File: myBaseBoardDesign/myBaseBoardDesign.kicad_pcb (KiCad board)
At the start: 2 copper layers, 100 x 100 mm, 14 parts, among them J1 BaseBoard, J2 Barrel_Jack_Switch, J4 Screw_Terminal_01x02, Q2 DMP6180SK3, SW1 SW_SPDT, U1 ESP32-S3-DevKitC

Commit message: Updated Tue Apr 2 2024 18:42
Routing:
- net GND: track 110.4 -> 147.2 mm, vias 83 -> 54
- net GP9: track 104.7 -> 141.4 mm, vias 1 -> 0
- net GP10: track 101.1 -> 136.0 mm, vias 1 -> 0
- net GP13: track 119.5 -> 101.2 mm
- net +5V: track 111.7 -> 128.7 mm, vias 2 -> 0
- net Net-(D1-A): track 21.9 -> 8.09 mm
- net GP46: track 127.9 -> 138.5 mm
- net GP5: track 106.7 -> 96.3 mm
- net GP7: track 87.2 -> 97.0 mm, vias 0 -> 2
- net GP15: track 49.8 -> 41.1 mm, vias 0 -> 1
- net GP16: track 49.8 -> 41.1 mm, vias 0 -> 1
- net GP47: track 76.3 -> 70.0 mm
- net GP40: track 88.6 -> 82.4 mm
- net GP8: track 106.4 -> 100.5 mm
- net GP2: track 91.8 -> 86.6 mm, vias 2 -> 1
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
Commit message: commit Apr 7 2024
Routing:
- net GP46: track 138.5 -> 121.7 mm, vias 0 -> 2
- net GP42: track 76.5 -> 82.6 mm
- net GND: track 147.2 -> 149.6 mm, vias 54 -> 130
- net GP21: track 88.8 -> 89.2 mm, vias 0 -> 1
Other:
- board text added: "+3V3"
- board text added: "+5V"
- board text added: "VIN"

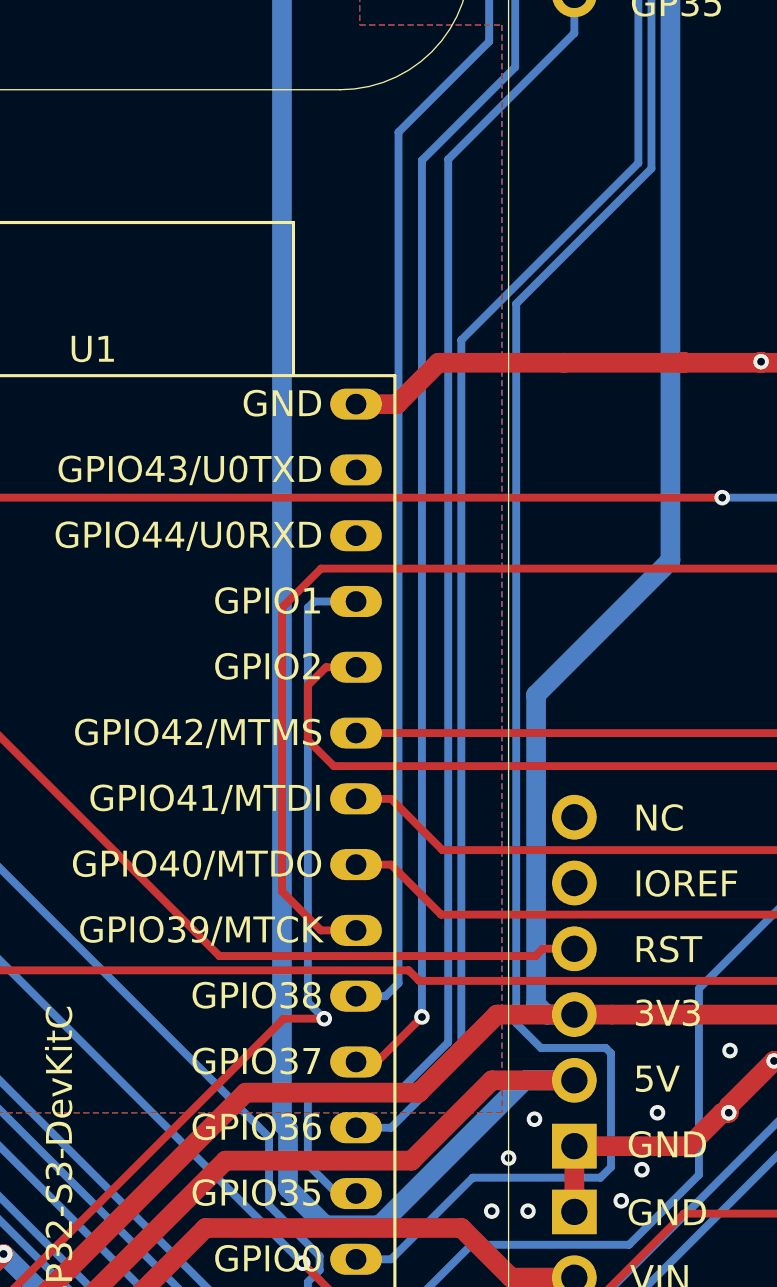
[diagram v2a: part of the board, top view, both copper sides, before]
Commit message: Sat: Apr 27 Added Dual H-Bridge Daughterboard and fixed railsplitter
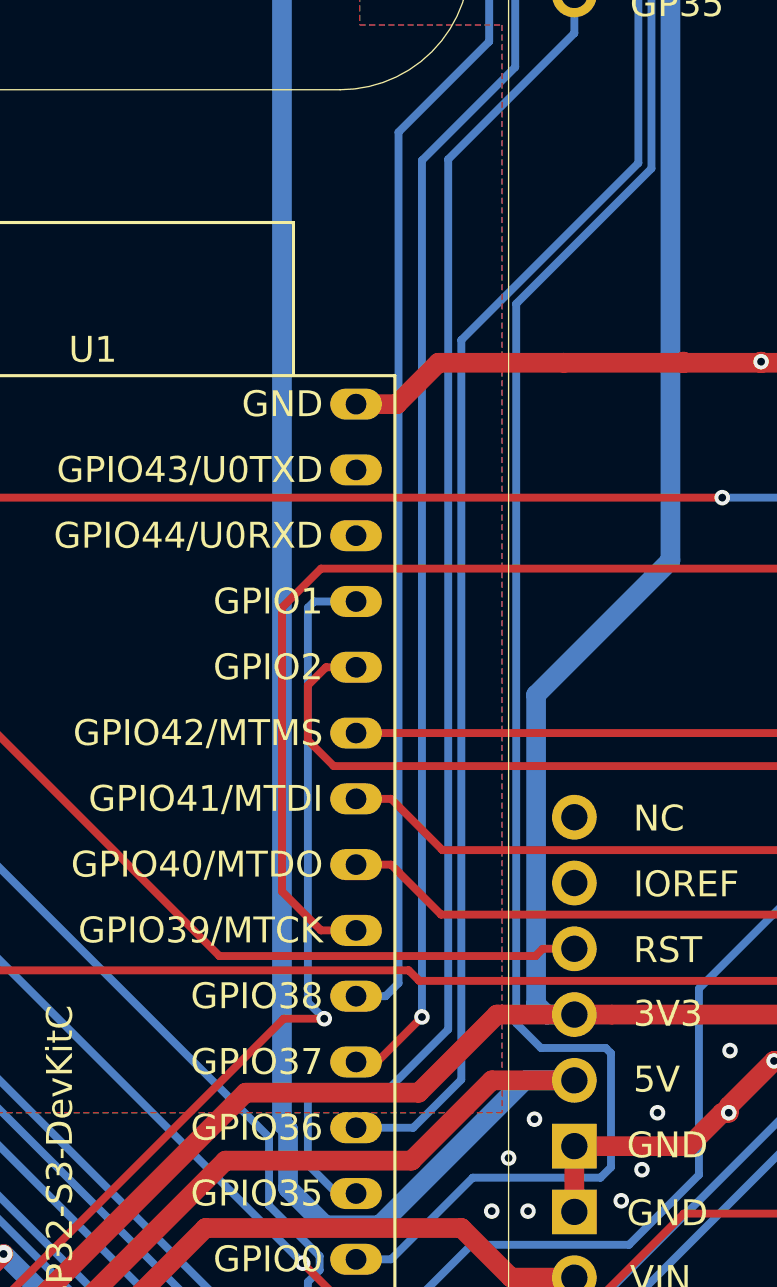
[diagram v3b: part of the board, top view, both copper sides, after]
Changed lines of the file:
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@@
+	)
+	(segment
+		(start 113.36 115.58)
+		(end 115.56705 115.58)
+		(width 0.3048)
+		(layer "B.Cu")
+		(net 10)
+	)
+	(segment
+		(start 117.4247 85.1677)
+		(end 124.2618 78.3306)
+		(width 0.3048)
+		(layer "B.Cu")
+		(net 10)
+	)
+	(segment
+		(start 124.2618 78.3306)
+		(end 124.2618 69.7618)
+		(width 0.3048)
+		(layer "B.Cu")
+		(net 10)
+	)
+	(segment
+		(start 123.8 69.3)
+		(end 121.79 69.3)
+		(width 0.3048)
+		(layer "B.Cu")
+		(net 10)
+	)
+	(segment
+		(start 115.56705 115.58)
+		(end 117.4247 113.72235)
+		(width 0.3048)
+		(layer "B.Cu")
+		(net 10)
+	)
+	(segment
+		(start 117.4247 113.72235)
+		(end 117.4247 85.1677)
+		(width 0.3048)
+		(layer "B.Cu")
+		(net 10)
 	)
 	(segment
 		(start 124.2618 69.7618)
 		(end 123.8 69.3)
-		(width 0.3048)
-		(layer "B.Cu")
-		(net 10)
-	)
-	(segment
-		(start 113.36 115.58)
-		(end 114.7141 115.58)
-		(width 0.3048)
-		(layer "B.Cu")
-		(net 10)
-	)
-	(segment
-		(start 124.2618 78.3306)
-		(end 124.2618 69.7618)
-		(width 0.3048)
-		(layer "B.Cu")
-		(net 10)
-	)
-	(segment
-		(start 117.4247 112.8694)
-		(end 117.4247 85.1677)
-		(width 0.3048)
-		(layer "B.Cu")
-		(net 10)
-	)
-	(segment
-		(start 123.8 69.3)
-		(end 121.79 69.3)
-		(width 0.3048)
-		(layer "B.Cu")
-		(net 10)
-	)
-	(segment
-		(start 117.4247 85.1677)
-		(end 124.2618 78.3306)
-		(width 0.3048)
-		(layer "B.Cu")
-		(net 10)
-	)
-	(segment
-		(start 114.7141 115.58)
-		(end 117.4247 112.8694)
 		(width 0.3048)
 		(layer "B.Cu")
@@
 	)
 	(segment
+		(start 116.9182 111.7818)
+		(end 114.5 114.2)
+		(width 0.3048)
+		(layer "B.Cu")
+		(net 31)
+	)
+	(segment
 		(start 121.79 71.84)
 		(end 121.79 73.3156)
@@
 	)
 	(segment
+		(start 112.62 118.12)
+		(end 113.36 118.12)
+		(width 0.3048)
+		(layer "B.Cu")
+		(net 31)
+	)
+	(segment
+		(start 114.5 114.2)
+		(end 111.8 114.2)
+		(width 0.3048)
+		(layer "B.Cu")
+		(net 31)
+	)
+	(segment
 		(start 111.5 117)
 		(end 112.62 118.12)
@@
 	)
 	(segment
-		(start 116.9182 112.2818)
-		(end 115 114.2)
-		(width 0.3048)
-		(layer "B.Cu")
-		(net 31)
-	)
-	(segment
-		(start 112.62 118.12)
-		(end 113.36 118.12)
-		(width 0.3048)
-		(layer "B.Cu")
-		(net 31)
-	)
-	(segment
 		(start 121.79 73.3156)
 		(end 116.9182 78.1874)
@@
 	)
 	(segment
-		(start 115 114.2)
-		(end 111.8 114.2)
-		(width 0.3048)
-		(layer "B.Cu")
-		(net 31)
-	)
-	(segment
 		(start 116.9182 78.1874)
-		(end 116.9182 112.2818)
-		(width 0.3048)
-		(layer "B.Cu")
+		(end 116.9182 111.7818)
+		(width 0.3048)
+		(layer "B.Cu")

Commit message: Sat Apr 27: fixed a few things. Finalized v0.2 baseboard and powerboard. Added logos.
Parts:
- added G***: LOGO, logos:heritage-logo, F.Cu at (145.0, 82.9)
- moved R4 4.75 mm to (82.2, 135.8)
- moved D4 4.74 mm to (76.0, 135.8)
- moved R3 3.96 mm to (82.3, 140.0), turned to 180 degrees
- moved D3 3.95 mm to (76.0, 140.0)
- moved R2 0.34 mm to (82.2, 131.6), turned to 180 degrees
- moved D1 0.20 mm to (76.2, 127.4)
- moved Q2 0.20 mm to (77.9, 121.0)
- moved D2 0.07 mm to (76.0, 131.6)
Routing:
- net +3V3: track 182.7 -> 165.3 mm
- net /PWRB: track 25.3 -> 17.3 mm
- net Net-(D2-A): track 7.58 -> 3.15 mm
- net Net-(D3-A): track 7.59 -> 3.29 mm
- net +5V: track 128.7 -> 127.3 mm
- net GND: vias 130 -> 147
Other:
- board text added: "+"
- board text added: "-"
- board text added: "Baseboard v0.2 Hussam Al-Hertani"

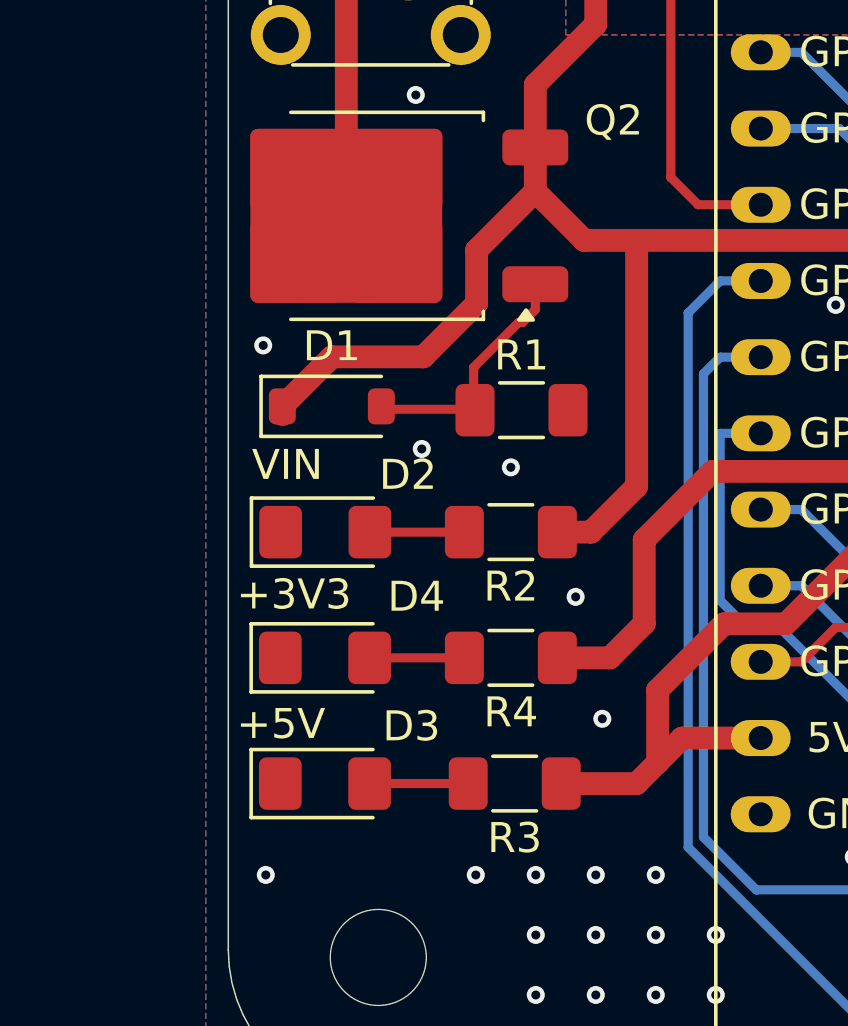
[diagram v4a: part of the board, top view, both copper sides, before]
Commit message: Added an improved version 0.2 Stereo Amp with heatsinks
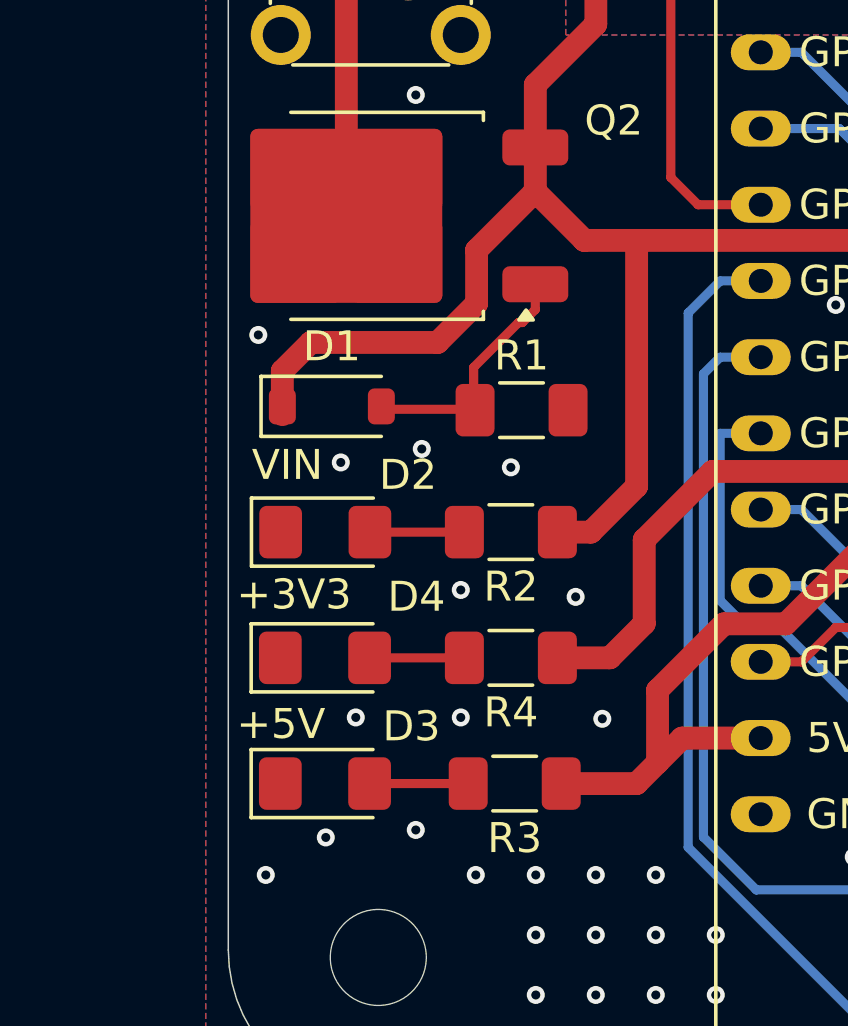
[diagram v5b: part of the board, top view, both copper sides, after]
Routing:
- net VIN: track 134.8 -> 135.5 mm
- net GND: vias 147 -> 153
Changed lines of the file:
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@@
+	)
+	(segment
+		(start 79.728 125.25)
+		(end 81.026 123.952)
+		(width 0.762)
+		(layer "F.Cu")
+		(net 2)
 	)
 	(segment
@@
 	)
 	(segment
-		(start 82.984 120.216)
-		(end 81.026 122.174)
-		(width 0.762)
-		(layer "F.Cu")
-		(net 2)
-	)
-	(segment
 		(start 74.55 60.46)
 		(end 74.55 61.73)
@@
 	)
 	(segment
-		(start 81.026 122.174)
-		(end 81.026 123.952)
-		(width 0.762)
-		(layer "F.Cu")
-		(net 2)
-	)
-	(segment
 		(start 84.6167 121.8487)
 		(end 82.984 120.216)
@@
 	)
 	(segment
-		(start 81.026 123.952)
-		(end 79.248 125.73)
-		(width 0.762)
-		(layer "F.Cu")
-		(net 2)
-	)
-	(segment
 		(start 84.836 131.572)
 		(end 86.36 130.048)
@@
 	)
 	(segment
-		(start 76.202 125.73)
-		(end 74.551 127.381)
-		(width 0.762)
-		(layer "F.Cu")
-		(net 2)
-	)
-	(segment
 		(start 74.551 127.381)
 		(end 74.551 127.656)
@@
 	)
 	(segment
+		(start 74.551 126.199)
+		(end 75.5 125.25)
+		(width 0.762)
+		(layer "F.Cu")
+		(net 2)
+	)
+	(segment
 		(start 74.55 61.73)
 		(end 75.73 61.73)
@@
 	)
 	(segment
+		(start 81.026 122.174)
+		(end 82.984 120.216)
+		(width 0.762)
+		(layer "F.Cu")
+		(net 2)
+	)
+	(segment
+		(start 75.5 125.25)
+		(end 79.728 125.25)
+		(width 0.762)
+		(layer "F.Cu")
+		(net 2)
+	)
+	(segment
 		(start 85 71)
 		(end 85 114.644)
@@
 	)
 	(segment
+		(start 81.026 123.952)
+		(end 81.026 122.174)
+		(width 0.762)
+		(layer "F.Cu")
+		(net 2)
+	)
+	(segment
 		(start 119.3502 121.37)
 		(end 117.4321 119.4519)
@@
 	)
 	(segment
-		(start 79.248 125.73)
-		(end 76.202 125.73)
+		(start 74.551 127.381)
+		(end 74.551 126.199)
 		(width 0.762)
 		(layer "F.Cu")
@@
 	)
 	(via
+		(at 76 141.75)
+		(size 0.6)
+		(drill 0.3)
+		(layers "F.Cu" "B.Cu")
+		(free yes)
+		(net 4)
+	)
+	(via
 		(at 145 60)
 		(size 0.6)
@@
 	)
 	(via
-		(at 73.914 125.349)
-		(size 0.6)
-		(drill 0.3)
-		(layers "F.Cu" "B.Cu")
-		(free yes)
-		(net 4)
-	)
-	(via
 		(at 81 143)
 		(size 0.6)
@@
 	)
 	(via
+		(at 76.5 129.25)
+		(size 0.6)
+		(drill 0.3)
+		(layers "F.Cu" "B.Cu")
+		(free yes)
+		(net 4)
+	)
+	(via
 		(at 135 65)
 		(size 0.6)
@@
 	(via
 		(at 124 132)
+		(size 0.6)
+		(drill 0.3)
+		(layers "F.Cu" "B.Cu")
+		(free yes)
+		(net 4)
+	)
+	(via
+		(at 80.5 133.5)
+		(size 0.6)
+		(drill 0.3)
+		(layers "F.Cu" "B.Cu")
+		(free yes)
+		(net 4)
+	)
+	(via
+		(at 77 137.75)
 		(size 0.6)
 		(drill 0.3)
@@
 	)
 	(via
+		(at 80.5 137.75)
+		(size 0.6)
+		(drill 0.3)
+		(layers "F.Cu" "B.Cu")
+		(free yes)
+		(net 4)
+	)
+	(via
 		(at 79.2 128.8)
 		(size 0.6)
@@
 	)
 	(via
+		(at 79 141.5)
+		(size 0.6)
+		(drill 0.3)
+		(layers "F.Cu" "B.Cu")
+		(free yes)
+		(net 4)
+	)
+	(via
 		(at 145 65)
 		(size 0.6)
@@
 		(size 0.6)
 		(drill 0.3)
+		(layers "F.Cu" "B.Cu")
+		(free yes)
+		(net 4)
+	)
+	(via
+		(at 73.75 125)
+		(size 0.6)
+		(drill 0.3)
